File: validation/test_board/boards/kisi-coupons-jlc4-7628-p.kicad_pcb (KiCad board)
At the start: 4 copper layers, 100 x 96 mm, 20 parts, among them J1 292-04A-14, J10 292-04A-14, J11 292-04A-14, J12 292-04A-14, J2 292-04A-14, J3 292-04A-14, J4 292-04A-14, J5 292-04A-14, J6 292-04A-14, J7 292-04A-14, J8 292-04A-14, J9 292-04A-14, U1 pin field (no part), U2 pin field (no part), U3 pin field (no part), U4 pin field (no part)

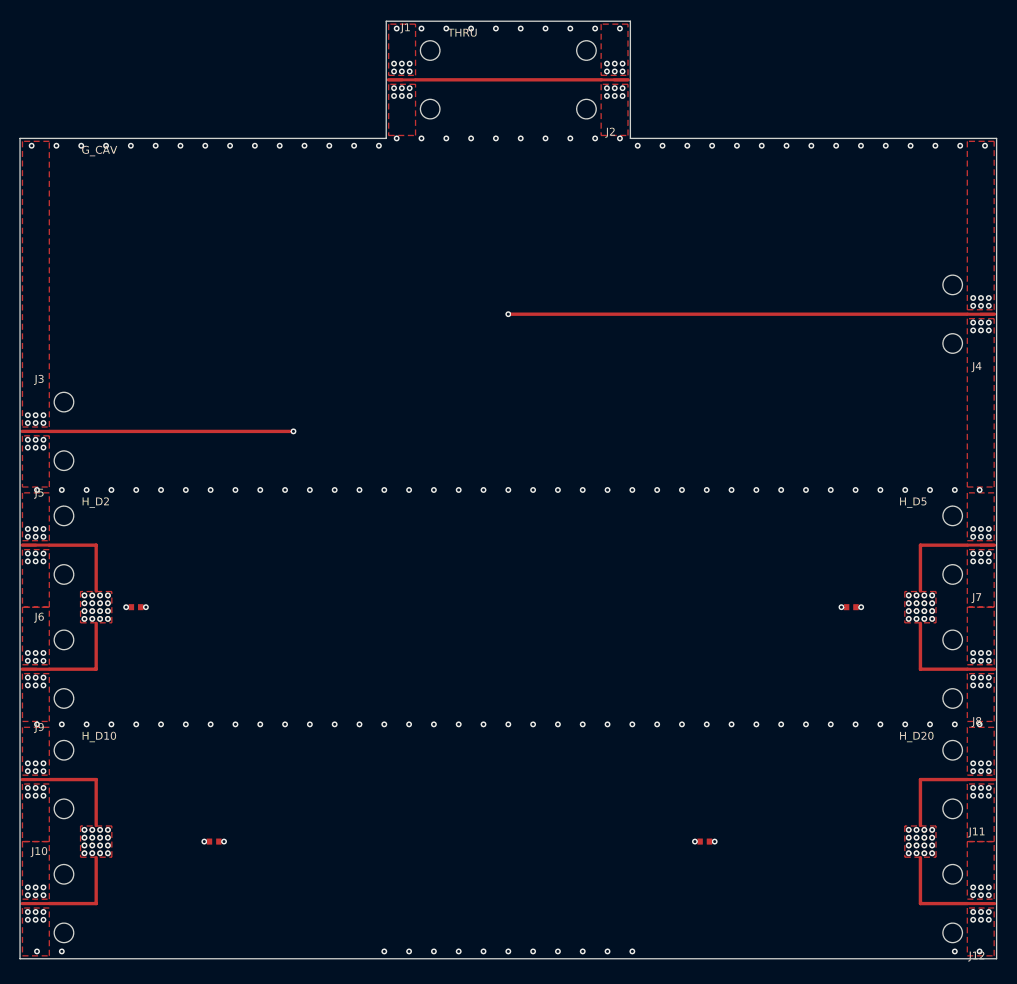
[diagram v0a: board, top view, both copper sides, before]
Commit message: Measurement coupons v3: Samtec 2.92 mm edge launch, 40 GHz plan
- Connector: Samtec 292-J-P-EP-ST-EL-01 (2.92 mm to 40 GHz, compression
  mount, PCB 1.02-2.54 mm; maintainer's decision 2026-10-30 on the RF
  group's advice) replaces the SMA Southwest 292-04A-14. Data, sources,
  the meaning of every footprint dimension of Samtec's drawing and the
  benchmark of Samtec's RF report (2023-06-01) in connectors.json.
- Footprint generated by make_coupons.py from parameters (Samtec's
  files are not committed: their terms forbid redistributing the
  models): geometry from drawing 292-J-P-EP-ST-EL-01-X-MKT rev C,
  plated screw holes 2.79 mm from the edge, +-2.92 mm, ground pads on
  top and bottom copper, signal tip 0.23 mm; marked DRAFT. The
  generator checks that no other net lies under the pads.
- Launch parametric (tip, taper, pad, coplanar section, ground cut,
  fence); default our 50 ohm coplanar launch inside the Samtec pads.
  --launch-cases writes kisi-fdtd cases; first runs (board side only)
  in fdtd_ref/launch_jlc4_7628: -18.9 dB worst to 40 GHz with the
  launch width to the edge, Samtec's 0.52 mm pad -14.6 dB.
- 40 GHz plan: stub notches of 6-layer VLV_L3 and 8-layer VLV_L6 now in
  the band, row via walls 2.54 -> 1.27 mm, measurement plan and ordering
  checklist to 40 GHz with 2.92 mm calibration and tools.
- Boards, manifests and 3D cases regenerated (widths unchanged); DRC
  with KiCad 7 on converted copies: no errors; kisi check rerun with
  kisi 0.3.1 (three v2 findings resolved in kisi since).

Co-Authored-By: Claude Opus 5.5 <noreply@anthropic.com>
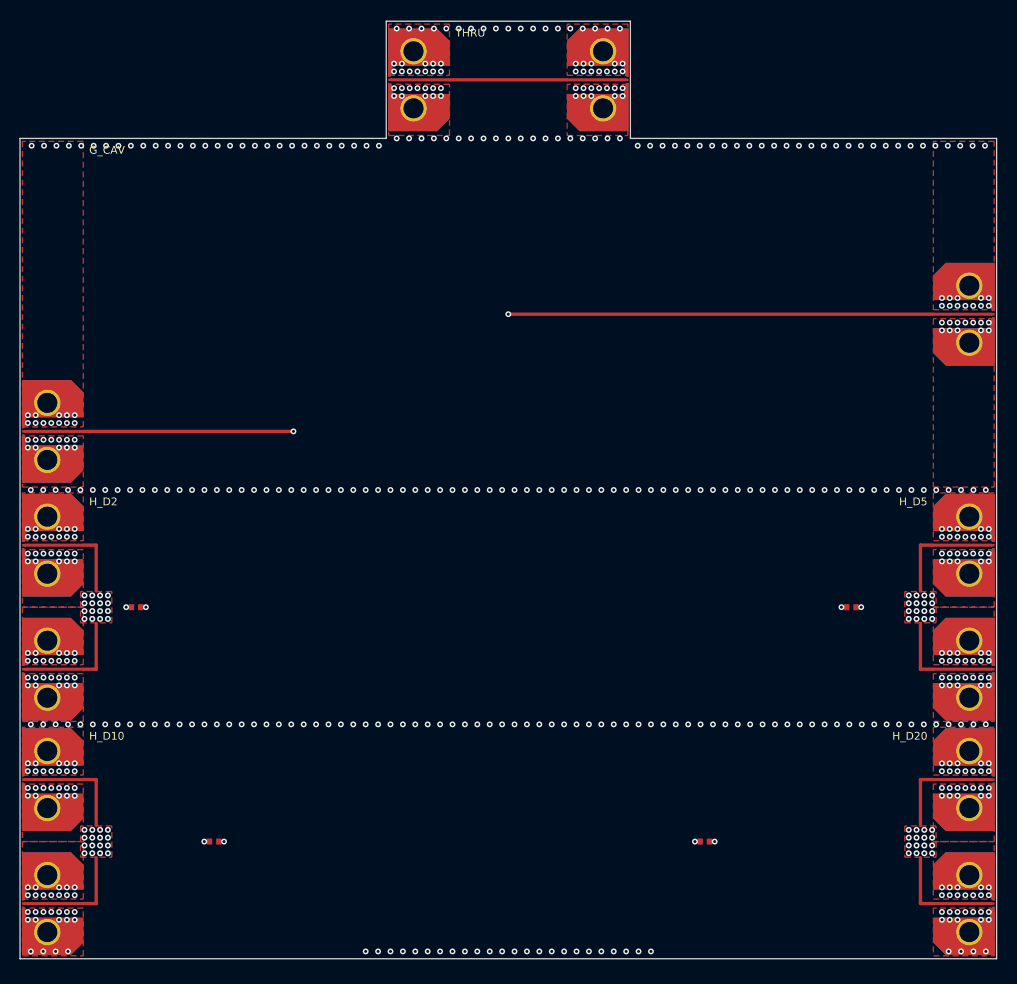
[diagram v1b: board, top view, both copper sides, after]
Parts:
- J1, J10, J11, J12, J2, J3, J4, J5, J6, J7, J8, J9: value 292-04A-14 -> 292-J-P-EP-ST-EL-01; footprint kisi_coupons:SWM_292-04A-14_EndLaunch_PLACEHOLDER -> kisi_coupons:Samtec_292-J-P-EP-ST-EL-01_EdgeLaunch
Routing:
- net VDD_H_D5: track 25.1 -> 23.9 mm
- net VDD_H_D20: track 25.1 -> 23.9 mm
- net CAV_G_CAV: track 77.6 -> 76.4 mm
- net VDD_H_D2: track 25.1 -> 23.9 mm
- net VDD_H_D10: track 25.1 -> 23.9 mm
- net SE_THRU: track 24.6 -> 23.4 mm
- net GND: vias 323 -> 608
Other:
- board text added: "2026-10-30"
- board text added: "Connector footprint generated from Samtec's drawing (DRAFT, connectors.json); launch not yet optimised."
- board text added: "Copper comes to 0.2 mm from the left/right edges at the 2.92 mm edge launches (Samtec 292-J-P-EP-ST-EL-01, plated screw holes)."
- board text added: "JLC04161H-7628 v3"
- board text added: "kisi-coupons-jlc4-7628-p: kisi measurement coupons v3 (2026-10-30)"
- board text removed: "Connector footprint is a PLACEHOLDER (connectors.json) until the vendor drawing is supplied."
- board text removed: "Copper comes to 0.2 mm from the left/right edges at the SMA end launches (Southwest Microwave 292-04A-14)."
- board text removed: "JLC04161H-7628 v2 2026-10-22"
- board text removed: "kisi-coupons-jlc4-7628-p: kisi measurement coupons v2 (2026-10-22)"

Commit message: Launch optimisation step 1: launch width to the edge, fence 0.55 mm
- kisi-fdtd launch cases on the 7628 stack, board side (the connector's
  coax not modelled): our 50 ohm coplanar launch run to the edge with a
  0.55 mm fence from 0.5 mm gives |S11| -21.0 dB at worst to 40 GHz;
  the 0.8 mm draft fence left |S21| dips at 25-38 GHz (-18.9 dB),
  Samtec's 0.23 mm tip -15.7 dB (-16.8 dB with the pin modelled), its
  0.52 mm pad -14.6 dB. These become the defaults in connectors.json;
  the variants are named after what they change, results in
  fdtd_ref/launch_jlc4_7628. The jaw case is still not valid.
- Boards regenerated with the new launch (DRC with KiCad 7: no errors),
  kisi check rerun.
- The connector is in stock at DigiKey (maintainer): the boards set the
  timeline.

Co-Authored-By: Claude Opus 5.5 <noreply@anthropic.com>
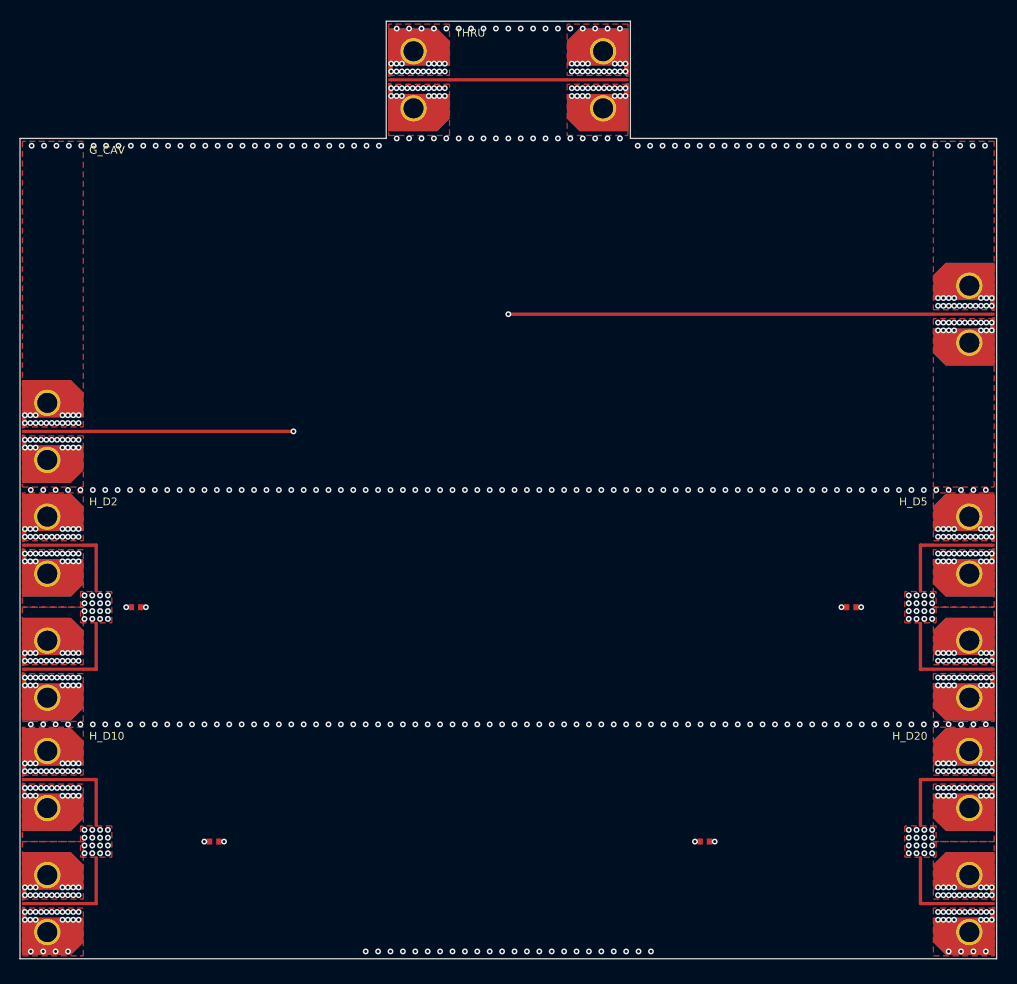
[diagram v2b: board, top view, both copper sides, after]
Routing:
- net GND: vias 608 -> 752
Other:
- board text added: "Connector footprint generated from Samtec's drawing (DRAFT, connectors.json); launch from a first kisi-fdtd optimisation step."
- board text removed: "Connector footprint generated from Samtec's drawing (DRAFT, connectors.json); launch not yet optimised."

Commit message: Coupon boards: own zone priorities, project-local footprint library
- KiCad 8/9 DRC reported overlapping zones of equal priority (the GND
  pour rectangles on L1 meet at 4-port launch pairs and along the CPWG
  coupons: 78 pairs on 26 boards). Every zone now has its own priority
  (planes 0, pours 1, 2, ..., islands and patches above); an outline
  check finds no equal-priority overlap left.
- The footprints the boards use are written as a project-local library
  (boards/kisi_coupons.pretty + fp-lib-table with ${KIPRJMOD}): the
  Samtec launch per launch width, the capacitor land patterns, the IC
  pin fields; per-instance Port/Status fields dropped, so board and
  library match. DRC (KiCad 7 on converted copies, with the library):
  no library warnings, no errors; the first-order boards are clean.
- Boards regenerated, kisi check unchanged.

Co-Authored-By: Claude Opus 5.5 <noreply@anthropic.com>
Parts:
- removed the J9 at (30.0, 107.7)
- added J8: 292-J-P-EP-ST-EL-01, kisi_coupons:Samtec_292-J-P-EP-ST-EL-01_EdgeLaunch_W0.315, F.Cu at (130.0, 96.3)
- C1, C2, C3, C4: footprint Capacitor_SMD:C_0402_1005Metric -> kisi_coupons:C_0402_1005Metric
- J1, J10, J11, J12, J2, J3, J4, J5, J6, J7: footprint kisi_coupons:Samtec_292-J-P-EP-ST-EL-01_EdgeLaunch -> kisi_coupons:Samtec_292-J-P-EP-ST-EL-01_EdgeLaunch_W0.315
- J9: renamed from J8; footprint kisi_coupons:Samtec_292-J-P-EP-ST-EL-01_EdgeLaunch -> kisi_coupons:Samtec_292-J-P-EP-ST-EL-01_EdgeLaunch_W0.315
- U1: footprint kisi_coupons:U -> kisi_coupons:U_VDD_H_D2
- U2: footprint kisi_coupons:U -> kisi_coupons:U_VDD_H_D5
- U3: footprint kisi_coupons:U -> kisi_coupons:U_VDD_H_D10
- U4: footprint kisi_coupons:U -> kisi_coupons:U_VDD_H_D20
- moved J9 100.6 mm to (30.0, 107.7), turned to 0 degrees
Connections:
- J9 pad 1: VDD_H_D5 -> VDD_H_D10
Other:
- board text added: "2026-10-31"
- board text added: "kisi-coupons-jlc4-7628-p: kisi measurement coupons v3 (2026-10-31)"
- board text removed: "2026-10-30"
- board text removed: "kisi-coupons-jlc4-7628-p: kisi measurement coupons v3 (2026-10-30)"
